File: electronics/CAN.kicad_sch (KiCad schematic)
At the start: 2 parts, among them J2 CAN, U3 TJA1051T-3

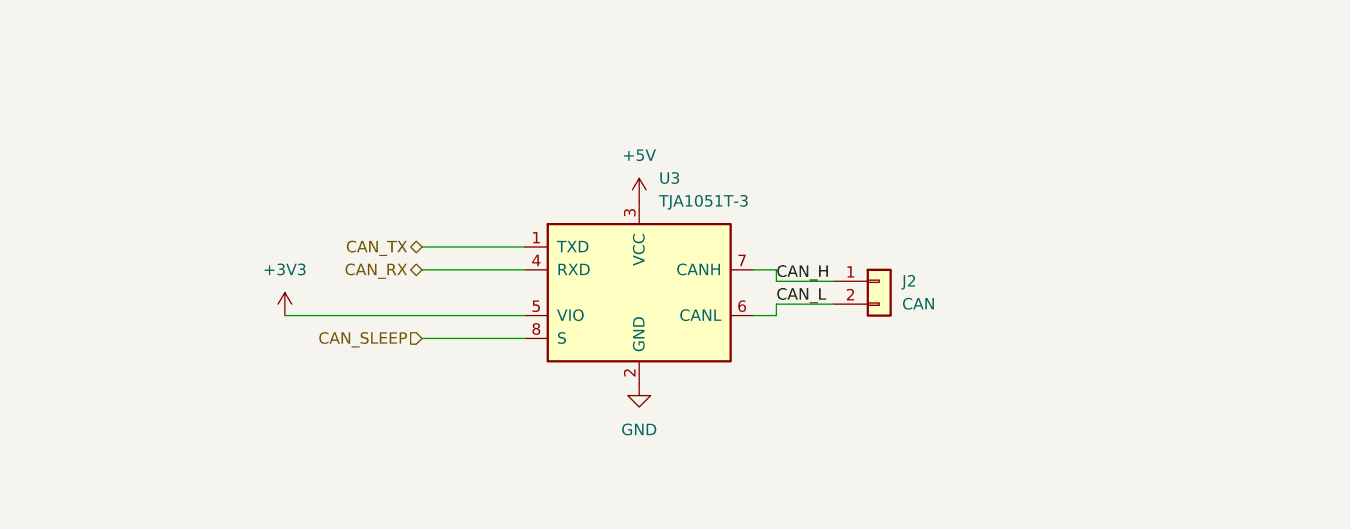
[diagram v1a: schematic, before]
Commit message: start to create BOM and finalising symbol fields
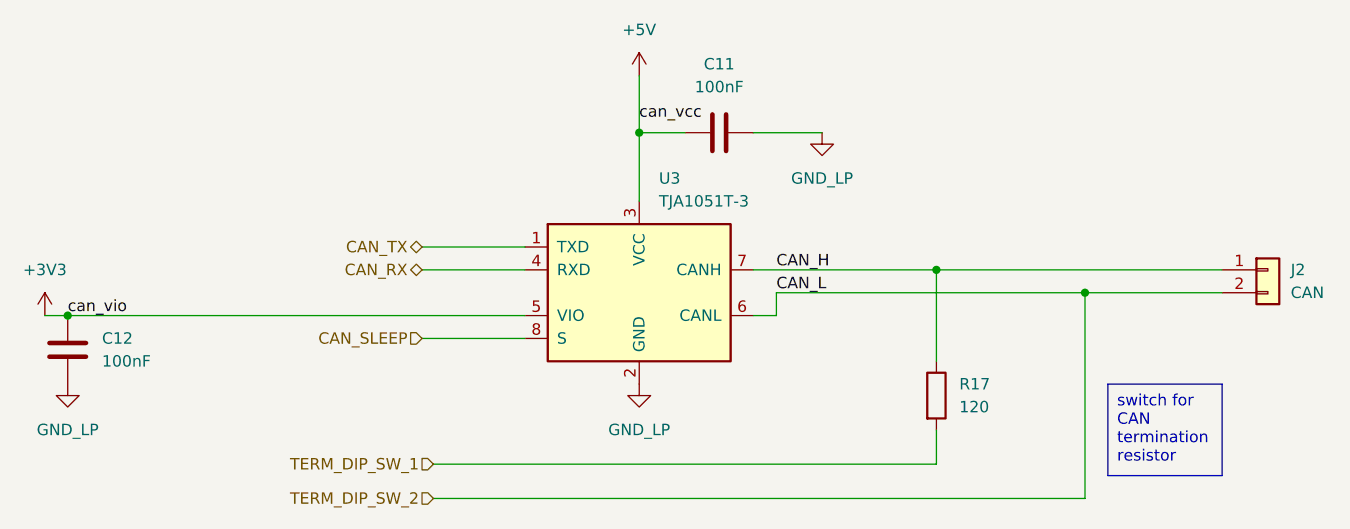
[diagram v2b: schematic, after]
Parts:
- added C11, C12: 100nF, Capacitor_SMD:C_0805_2012Metric, symbol Device:C
- added R17: 120, Resistor_SMD:R_0805_2012Metric, symbol Device:R
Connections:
- net +5V: now also C11.1
- net CAN_H: now also R17.1
- net can_vio: now reaches U3.5 (VIO)
- net can_vio: now also C12.1
- net CAN_L renamed TERM_DIP_SW_2
- net GND renamed GND_LP
- net GND_LP: now also C11.2, C12.2
- new net TERM_DIP_SW_1: R17.2
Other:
- moved on the sheet: J2
